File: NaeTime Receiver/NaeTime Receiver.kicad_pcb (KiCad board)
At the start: 2 copper layers, 135 x 140 mm, 22 parts, among them U15 RX5808_Breakout, U16 RX5808_Breakout, U17 RX5808_Breakout, U18 RX5808_Breakout, U19 RX5808_Breakout, U20 RX5808_Breakout, U21 RX5808_Breakout, U22 RX5808_Breakout

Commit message: Receiver pcb
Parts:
- removed the REF** at (100.0, 20.0)
- removed the REF** at (100.0, 145.0)
- removed the REF** at (215.0, 145.0)
- removed the REF** at (215.0, 20.0)
- removed U5: ~, NaeTimeComponentLibrary:RGB LED Header
- removed U6: ~, NaeTimeComponentLibrary:DPad Pin Header
- added D1: CLV1L-FKB, NaeTimeComponentLibrary:LED_D5.0mm-4_RGB GBCR, F.Cu at (176.1, 22.0)
- added D2: CLV1L-FKB, NaeTimeComponentLibrary:LED_D5.0mm-4_RGB GBCR, F.Cu at (19.7, 22.0)
- added D3: CLV1L-FKB, NaeTimeComponentLibrary:LED_D5.0mm-4_RGB GBCR, F.Cu at (176.2, 170.0)
- added D4: CLV1L-FKB, NaeTimeComponentLibrary:LED_D5.0mm-4_RGB GBCR, F.Cu at (20.2, 170.0)
- added QB1: BS170, Package_TO_SOT_THT:TO-92_Inline, F.Cu at (50.5, 20.0)
- added QG1: BS170, Package_TO_SOT_THT:TO-92_Inline, F.Cu at (56.5, 20.0)
- added QR1: BS170, Package_TO_SOT_THT:TO-92_Inline, F.Cu at (62.5, 20.0)
- added R1: R2, Resistor_THT:R_Axial_DIN0204_L3.6mm_D1.6mm_P7.62mm_Horizontal, F.Cu at (164.2, 19.0)
- added R10: R2, Resistor_THT:R_Axial_DIN0204_L3.6mm_D1.6mm_P7.62mm_Horizontal, F.Cu at (35.6, 167.0)
- added R11: R3, Resistor_THT:R_Axial_DIN0204_L3.6mm_D1.6mm_P7.62mm_Horizontal, F.Cu at (35.6, 170.0)
- added R12: R4, Resistor_THT:R_Axial_DIN0204_L3.6mm_D1.6mm_P7.62mm_Horizontal, F.Cu at (35.6, 173.0)
- added R13: R1, Resistor_THT:R_Axial_DIN0204_L3.6mm_D1.6mm_P7.62mm_Horizontal, F.Cu at (134.0, 149.0)
- added R14: R1, Resistor_THT:R_Axial_DIN0204_L3.6mm_D1.6mm_P7.62mm_Horizontal, F.Cu at (134.0, 124.0)
- added R15: R1, Resistor_THT:R_Axial_DIN0204_L3.6mm_D1.6mm_P7.62mm_Horizontal, F.Cu at (134.0, 99.0)
- added R16: R1, Resistor_THT:R_Axial_DIN0204_L3.6mm_D1.6mm_P7.62mm_Horizontal, F.Cu at (134.0, 74.0)
- added R17: R1, Resistor_THT:R_Axial_DIN0204_L3.6mm_D1.6mm_P7.62mm_Horizontal, F.Cu at (66.4, 103.0)
- added R18: R1, Resistor_THT:R_Axial_DIN0204_L3.6mm_D1.6mm_P7.62mm_Horizontal, F.Cu at (66.4, 128.0)
- added R19: R1, Resistor_THT:R_Axial_DIN0204_L3.6mm_D1.6mm_P7.62mm_Horizontal, F.Cu at (66.4, 153.0)
- added R2: R3, Resistor_THT:R_Axial_DIN0204_L3.6mm_D1.6mm_P7.62mm_Horizontal, F.Cu at (164.2, 22.0)
- added R20: R1, Resistor_THT:R_Axial_DIN0204_L3.6mm_D1.6mm_P7.62mm_Horizontal, F.Cu at (66.4, 78.0)
- added R3: R4, Resistor_THT:R_Axial_DIN0204_L3.6mm_D1.6mm_P7.62mm_Horizontal, F.Cu at (164.2, 25.0)
- added R4: R2, Resistor_THT:R_Axial_DIN0204_L3.6mm_D1.6mm_P7.62mm_Horizontal, F.Cu at (36.0, 19.0)
- added R5: R3, Resistor_THT:R_Axial_DIN0204_L3.6mm_D1.6mm_P7.62mm_Horizontal, F.Cu at (36.0, 22.0)
- added R6: R4, Resistor_THT:R_Axial_DIN0204_L3.6mm_D1.6mm_P7.62mm_Horizontal, F.Cu at (36.0, 25.0)
- added R7: R2, Resistor_THT:R_Axial_DIN0204_L3.6mm_D1.6mm_P7.62mm_Horizontal, F.Cu at (164.0, 167.0)
- added R8: R3, Resistor_THT:R_Axial_DIN0204_L3.6mm_D1.6mm_P7.62mm_Horizontal, F.Cu at (164.0, 170.0)
- added R9: R4, Resistor_THT:R_Axial_DIN0204_L3.6mm_D1.6mm_P7.62mm_Horizontal, F.Cu at (164.0, 173.0)
- added REF**: MountingHole_3.2mm_M3, MountingHole:MountingHole_3.2mm_M3, F.Cu at (135.0, 55.0)
- added REF**: MountingHole_3.2mm_M3, MountingHole:MountingHole_3.2mm_M3, F.Cu at (150.0, 25.0)
- added REF**: MountingHole_3.2mm_M3, MountingHole:MountingHole_3.2mm_M3, F.Cu at (135.0, 165.0)
- added REF**: MountingHole_3.2mm_M3, MountingHole:MountingHole_3.2mm_M3, F.Cu at (165.0, 55.0)
- added REF**: MountingHole_3.2mm_M3, MountingHole:MountingHole_3.2mm_M3, F.Cu at (20.0, 35.0)
- added REF**: MountingHole_3.2mm_M3, MountingHole:MountingHole_3.2mm_M3, F.Cu at (65.0, 165.0)
- added SW1: SW_Push, Button_Switch_THT:SW_PUSH_6mm_H5mm, F.Cu at (149.8, 31.8)
- added SW2: SW_Push, Button_Switch_THT:SW_PUSH_6mm_H5mm, F.Cu at (160.0, 40.5)
- added SW3: SW_Push, Button_Switch_THT:SW_PUSH_6mm_H5mm, F.Cu at (139.7, 40.5)
- added SW4: SW_Push, Button_Switch_THT:SW_PUSH_6mm_H5mm, F.Cu at (149.8, 49.0)
- moved U7 124.7 mm to (100.5, 20.0), turned to 90 degrees
- moved U1 115.3 mm to (42.5, 43.3), turned to -90 degrees
- moved U8 105.8 mm to (100.5, 171.0), turned to 90 degrees
- moved U19 83.1 mm to (40.0, 75.7)
- moved U20 82.2 mm to (40.0, 100.7)
- moved U21 81.0 mm to (40.0, 125.7)
- moved U22 79.3 mm to (40.0, 150.7)
- moved LS1 70.0 mm to (135.2, 25.0), turned to 0 degrees
- moved U2 62.6 mm to (92.2, 130.4)
- moved G*** 60.7 mm to (122.0, 161.0)
- moved U3 60.4 mm to (73.1, 40.6), turned to 0 degrees
- moved U4 58.6 mm to (79.0, 169.0)
- moved U15 53.8 mm to (160.0, 76.0)
- moved U16 52.5 mm to (160.0, 100.9)
- moved U17 50.6 mm to (160.0, 126.0)
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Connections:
- LS1 pad 1: GND -> Net-(LS1-Pad1)
- LS1 pad 2: Net-(LS1-Pad2) -> GND
- U1 pad 13: Net-(LS1-Pad2) -> Net-(LS1-Pad1)
- U1 pad 16: unconnected-(U1-23/MOSI-Pad16) -> Net-(U1-23/MOSI)
- U1 pad 17: Net-(U1-22/SCL) -> RED SWITCH
- U1 pad 20: unconnected-(U1-21/MISO-Pad20) -> Net-(U1-21/MISO)
- U1 pad 21: Net-(U1-19/MISO) -> Net-(U1-19/SCK)
- U1 pad 22: Net-(U1-18/SCK) -> unconnected-(U1-18-Pad22)
- U1 pad 6: Net-(U1-32) -> GREEN SWITCH
- U1 pad 7: Net-(U1-33) -> BLUE SWITCH
- U3 pad 3: Net-(U1-18/SCK) -> Net-(U1-19/SCK)
- U3 pad 4: Net-(U1-19/MISO) -> Net-(U1-21/MISO)
- U3 pad 8: +3.3V -> Net-(U1-23/MOSI)
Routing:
- net BLUE: track 0.00 -> 451.0 mm, vias 0 -> 4
- net GREEN: track 0.00 -> 447.0 mm, vias 0 -> 3
- net RED: track 0.00 -> 445.3 mm
- net Net-(U1-26): track 19.3 -> 209.6 mm, vias 0 -> 1
- net +5V: track 542.6 -> 723.8 mm
- net Net-(U1-25): track 22.9 -> 201.6 mm
- net Net-(U1-27): track 16.0 -> 192.7 mm, vias 0 -> 1
- net Net-(U1-14): track 12.1 -> 181.7 mm
- net Net-(LS1-Pad1): track 0.00 -> 111.1 mm, vias 0 -> 4
- net Net-(U1-32): track 82.1 -> 0.00 mm
- net Net-(U1-33): track 77.5 -> 0.00 mm
- net Net-(U1-22/SCL): track 52.4 -> 0.00 mm
- net Net-(U1-23/MOSI): track 0.00 -> 48.2 mm, vias 0 -> 2
- net GND: track 0.00 -> 46.4 mm, vias 0 -> 5
- net RED SWITCH: track 0.00 -> 45.1 mm, vias 0 -> 1
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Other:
- board size 135 x 140 mm -> 170 x 160 mm
- board text removed: "5V"
- board text removed: "The Swiss Cheese"
- board text removed: "V3"

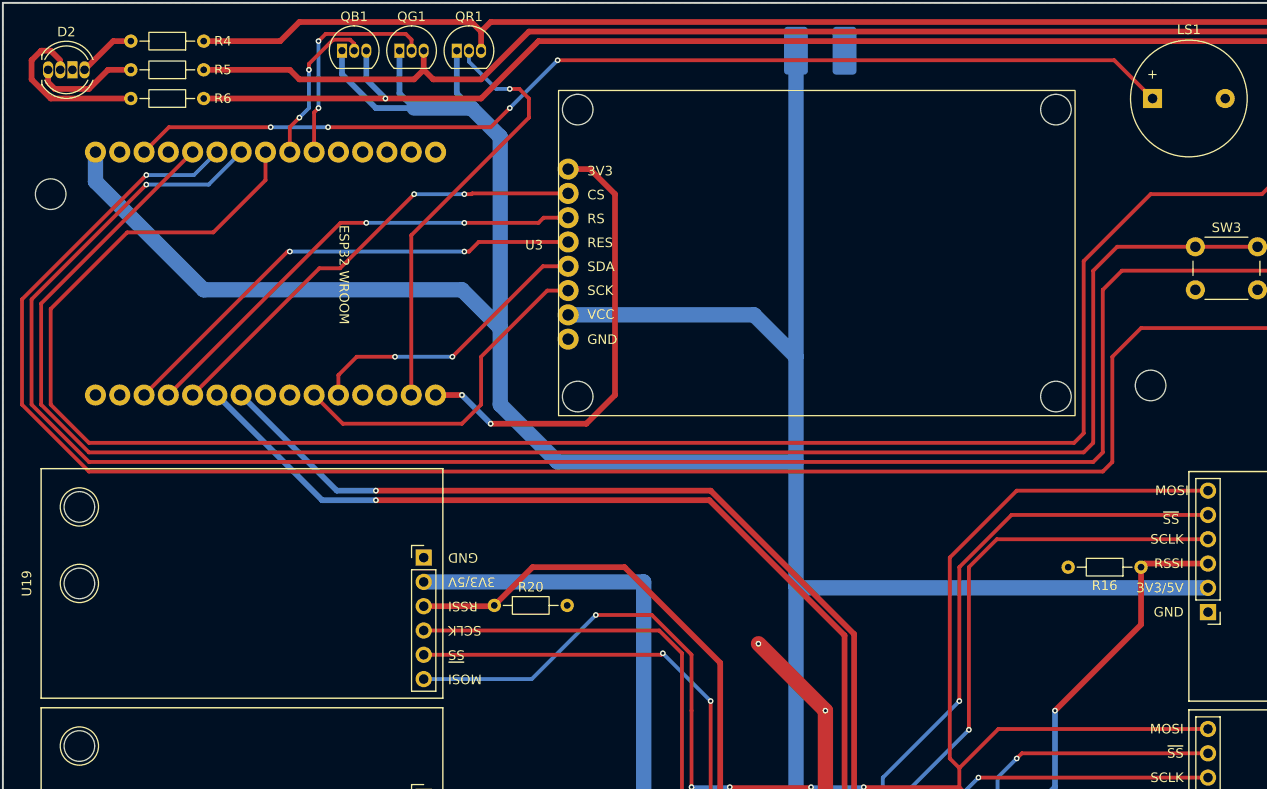
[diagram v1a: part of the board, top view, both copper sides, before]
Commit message: Fab and node menu
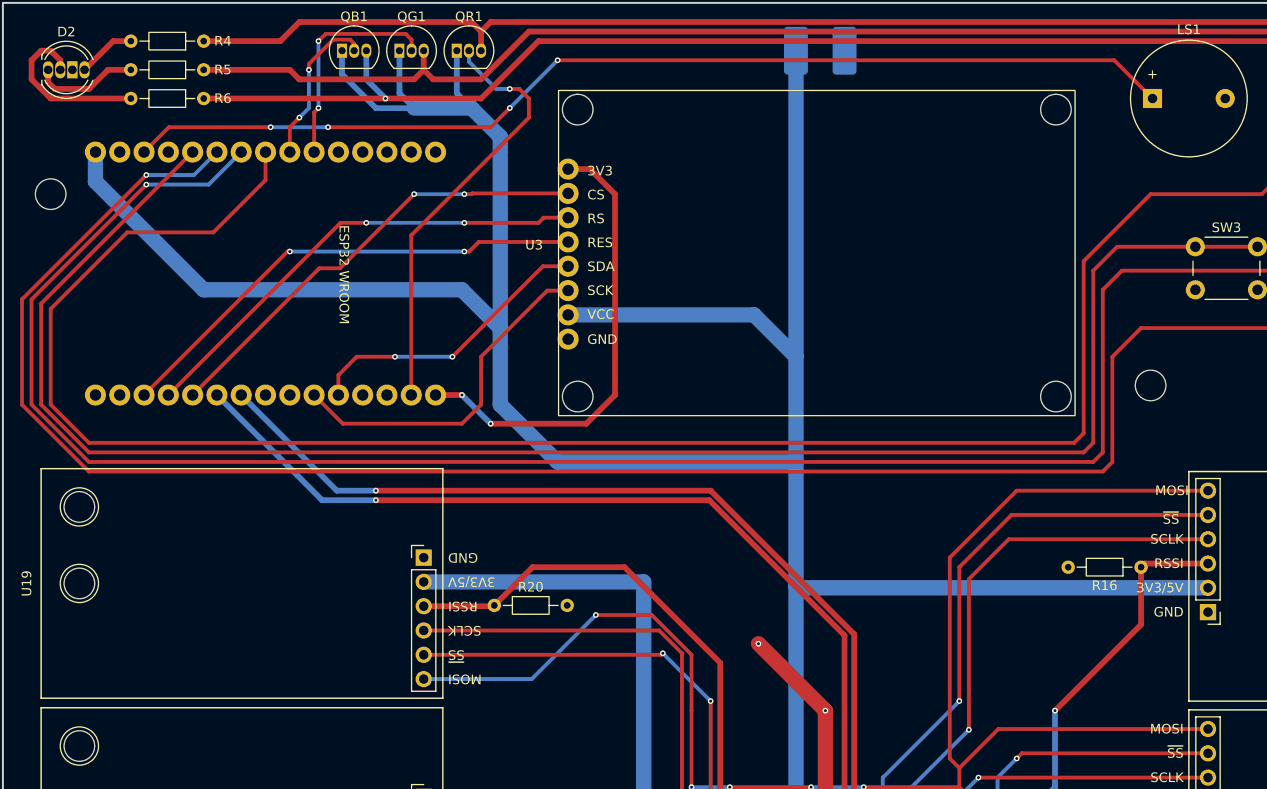
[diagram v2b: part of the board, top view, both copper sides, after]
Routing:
- net RSCLK: track 389.8 -> 389.1 mm
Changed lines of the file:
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@@
+	)
+	(segment
+		(start 116 75.25)
+		(end 116 91)
+		(width 0.4)
+		(layer "F.Cu")
+		(net 14)
+	)
+	(segment
+		(start 141 71.08)
+		(end 120.17 71.08)
+		(width 0.4)
+		(layer "F.Cu")
+		(net 14)
 	)
 	(segment
@@
 	)
 	(segment
-		(start 141 71.08)
-		(end 118.92 71.08)
-		(width 0.4)
-		(layer "F.Cu")
-		(net 14)
-	)
-	(segment
-		(start 118.92 71.08)
-		(end 116 74)
-		(width 0.4)
-		(layer "F.Cu")
-		(net 14)
-	)
-	(segment
 		(start 116 143)
 		(end 116 119)
@@
 	)
 	(segment
-		(start 116 74)
-		(end 116 91)
-		(width 0.4)
-		(layer "F.Cu")
-		(net 14)
-	)
-	(segment
 		(start 59 155.62)
 		(end 76.38 155.62)
@@
 		(start 116 99)
 		(end 115 98)
+		(width 0.4)
+		(layer "F.Cu")
+		(net 14)
+	)
+	(segment
+		(start 120.17 71.08)
+		(end 116 75.25)
 		(width 0.4)
 		(layer "F.Cu")
@@
 		(start 21 21)
 		(end 21 22)
-		(width 0.4)
+		(width 0.6)
 		(layer "F.Cu")
 		(net 62)
